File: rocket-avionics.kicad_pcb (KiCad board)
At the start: 2 copper layers, 20.3 x 45.7 mm, 37 parts, among them J1 Conn_01x02_Female, J2 Micro_SD_Card, J3 AVR-ISP-6, U1 AP2111H-3.3, U2 ATmega328P-AU, U3 MPU-6050, U4 BMP280_Module, Y1 8MHz Crystal

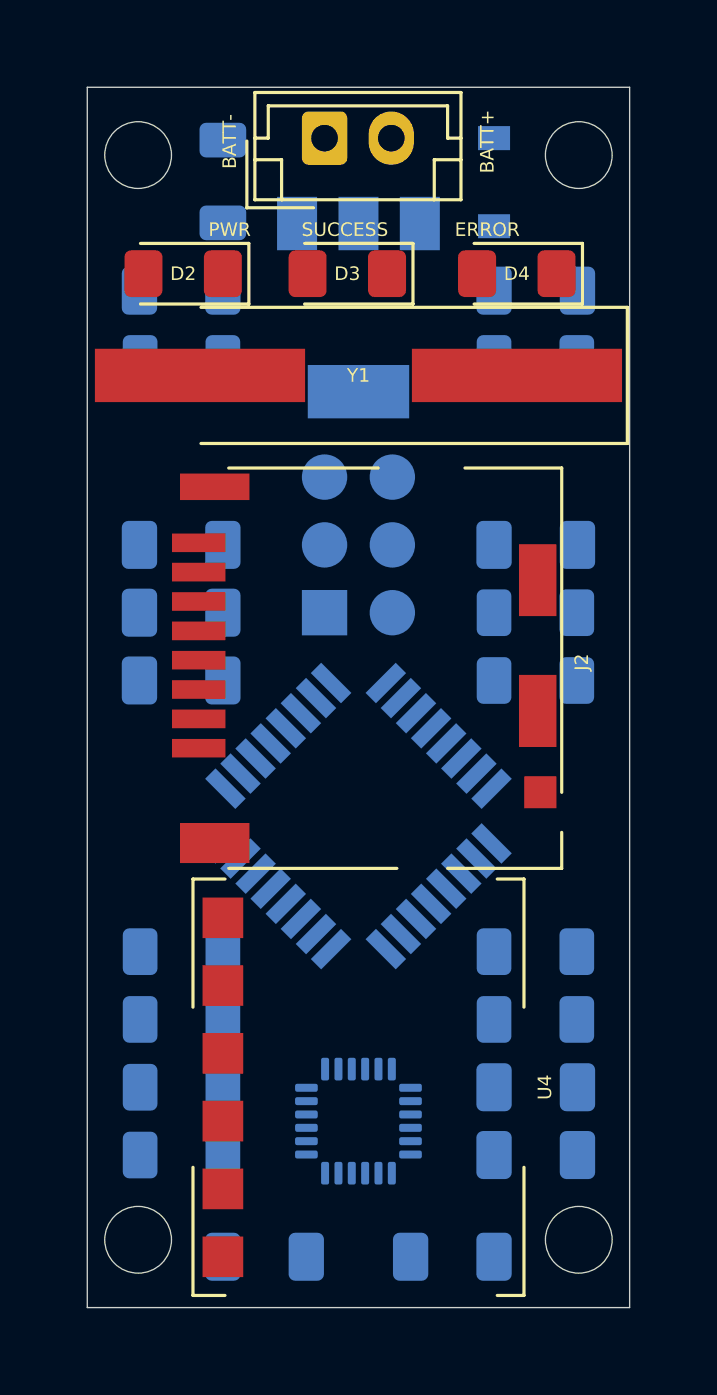
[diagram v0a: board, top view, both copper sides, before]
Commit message: Add traces and text to PCB layout.
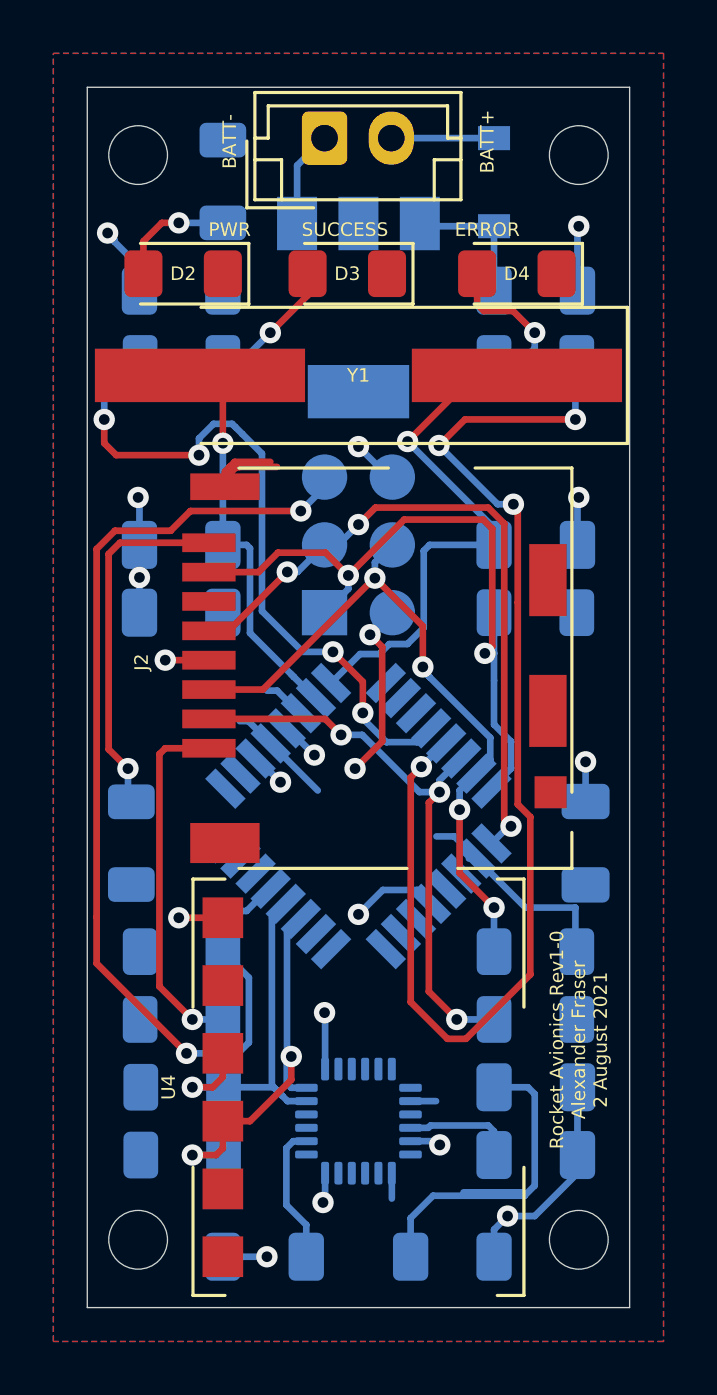
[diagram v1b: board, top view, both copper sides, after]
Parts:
- removed the REF** at (93.3, 120.7)
- removed the REF** at (109.9, 120.7)
- removed the REF** at (109.9, 80.0)
- removed the REF** at (93.3, 80.0)
- added REF**: MountingHole_2.2mm_M2, MountingHole:MountingHole_2.2mm_M2, F.Cu at (93.3, 120.7)
- added REF**: MountingHole_2.2mm_M2, MountingHole:MountingHole_2.2mm_M2, F.Cu at (109.9, 120.7)
- added REF**: MountingHole_2.2mm_M2, MountingHole:MountingHole_2.2mm_M2, F.Cu at (109.9, 80.0)
- added REF**: MountingHole_2.2mm_M2, MountingHole:MountingHole_2.2mm_M2, F.Cu at (93.3, 80.0)
- moved R1 17.4 mm to (93.1, 105.8), turned to 270 degrees
- moved C4 16.3 mm to (110.1, 105.8), turned to 90 degrees
- moved R10 2.54 mm to (95.0, 114.9)
- moved R11 2.54 mm to (95.0, 117.5)
- moved R2 2.54 mm to (108.2, 97.2)
- moved J2 0.38 mm to (101.3, 99.1)
- turned R3 to 90 degrees
- turned R5 to 0 degrees
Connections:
- C5 pad 1: ExtClock1 -> ExtClock2
- C6 pad 1: Net-(C6-Pad1) -> ExtClock1
- Y1 pad 1: ExtClock1 -> ExtClock2
- Y1 pad 2: Net-(C6-Pad1) -> ExtClock1
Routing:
- net ErrorLED: track 0.00 -> 45.7 mm, vias 0 -> 4
- net GND: track 0.00 -> 44.0 mm, vias 0 -> 15
- net +3V3: track 0.00 -> 39.9 mm, vias 0 -> 4
- net Reset: track 0.00 -> 39.8 mm, vias 0 -> 2
- net SPI-MISO: track 0.00 -> 27.1 mm, vias 0 -> 2
- net SuccessLED: track 0.00 -> 27.0 mm, vias 0 -> 4
- net SPI-MOSI: track 0.00 -> 26.3 mm, vias 0 -> 4
- net SPI-SCK: track 0.00 -> 25.7 mm, vias 0 -> 3
- net SPI-SS: track 0.00 -> 21.9 mm, vias 0 -> 3
- net ExtClock2: track 0.00 -> 21.9 mm, vias 0 -> 1
- net ExtClock1: track 0.00 -> 18.4 mm, vias 0 -> 1
- net I2C-Data: track 0.00 -> 15.8 mm, vias 0 -> 2
- net I2C-Clock: track 0.00 -> 14.3 mm, vias 0 -> 1
- net Net-(J2-Pad8): track 0.00 -> 13.6 mm, vias 0 -> 1
- net Net-(J2-Pad1): track 0.00 -> 13.2 mm, vias 0 -> 1
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- added copper zone on B.Cu, net +3V3
- added copper zone on F.Cu, net GND
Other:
- board text added: "."
- board text added: "GND"
- board text added: "MISO"
- board text added: "MOSI"
- board text added: "RST"
- board text added: "Rocket Avionics Rev1-0 Alexander Fraser 2 August 2021"
- board text added: "SCK"
- board text added: "VCC"

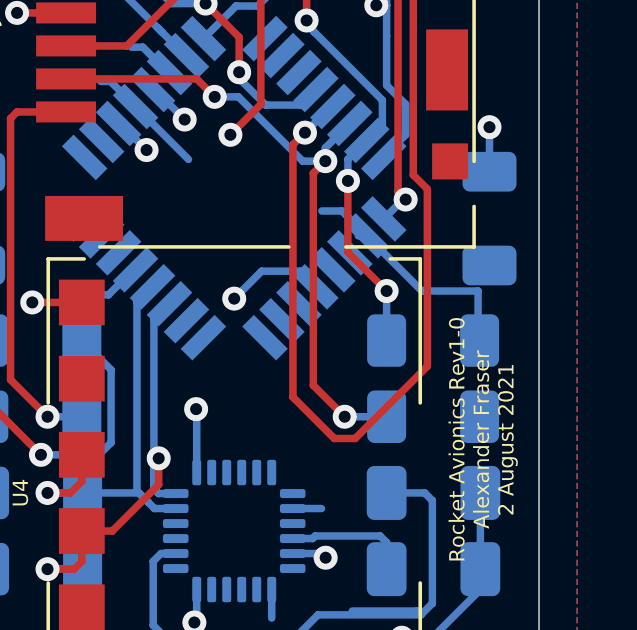
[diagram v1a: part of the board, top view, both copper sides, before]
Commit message: Clean up of copper pours in PCB layout.
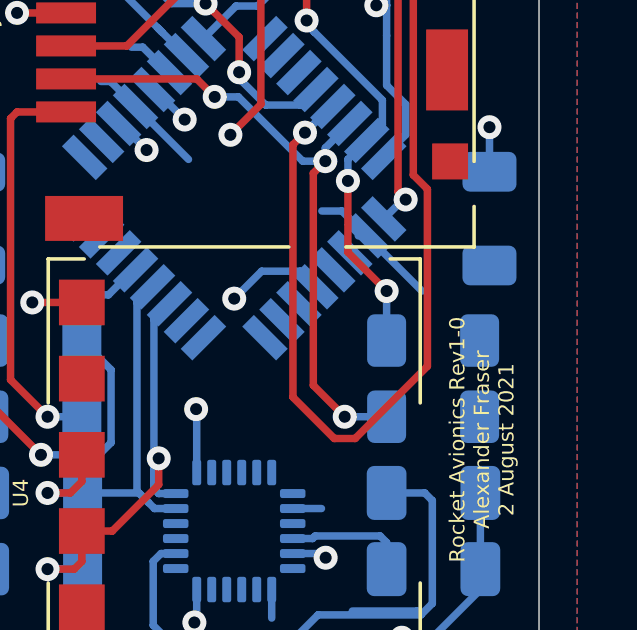
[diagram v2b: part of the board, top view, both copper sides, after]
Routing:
- net +3V3: track 39.9 -> 36.5 mm
